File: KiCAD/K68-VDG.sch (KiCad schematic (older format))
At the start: 39 parts, among them J1 Video Out, J2 SBC6303 BUS, Q1 2SA1015, Q2 2SC1815, U1 MC6847, U2 MC1372, U3 74LS32, U4 74HCT573, U5 74LS02, U6 74LS244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

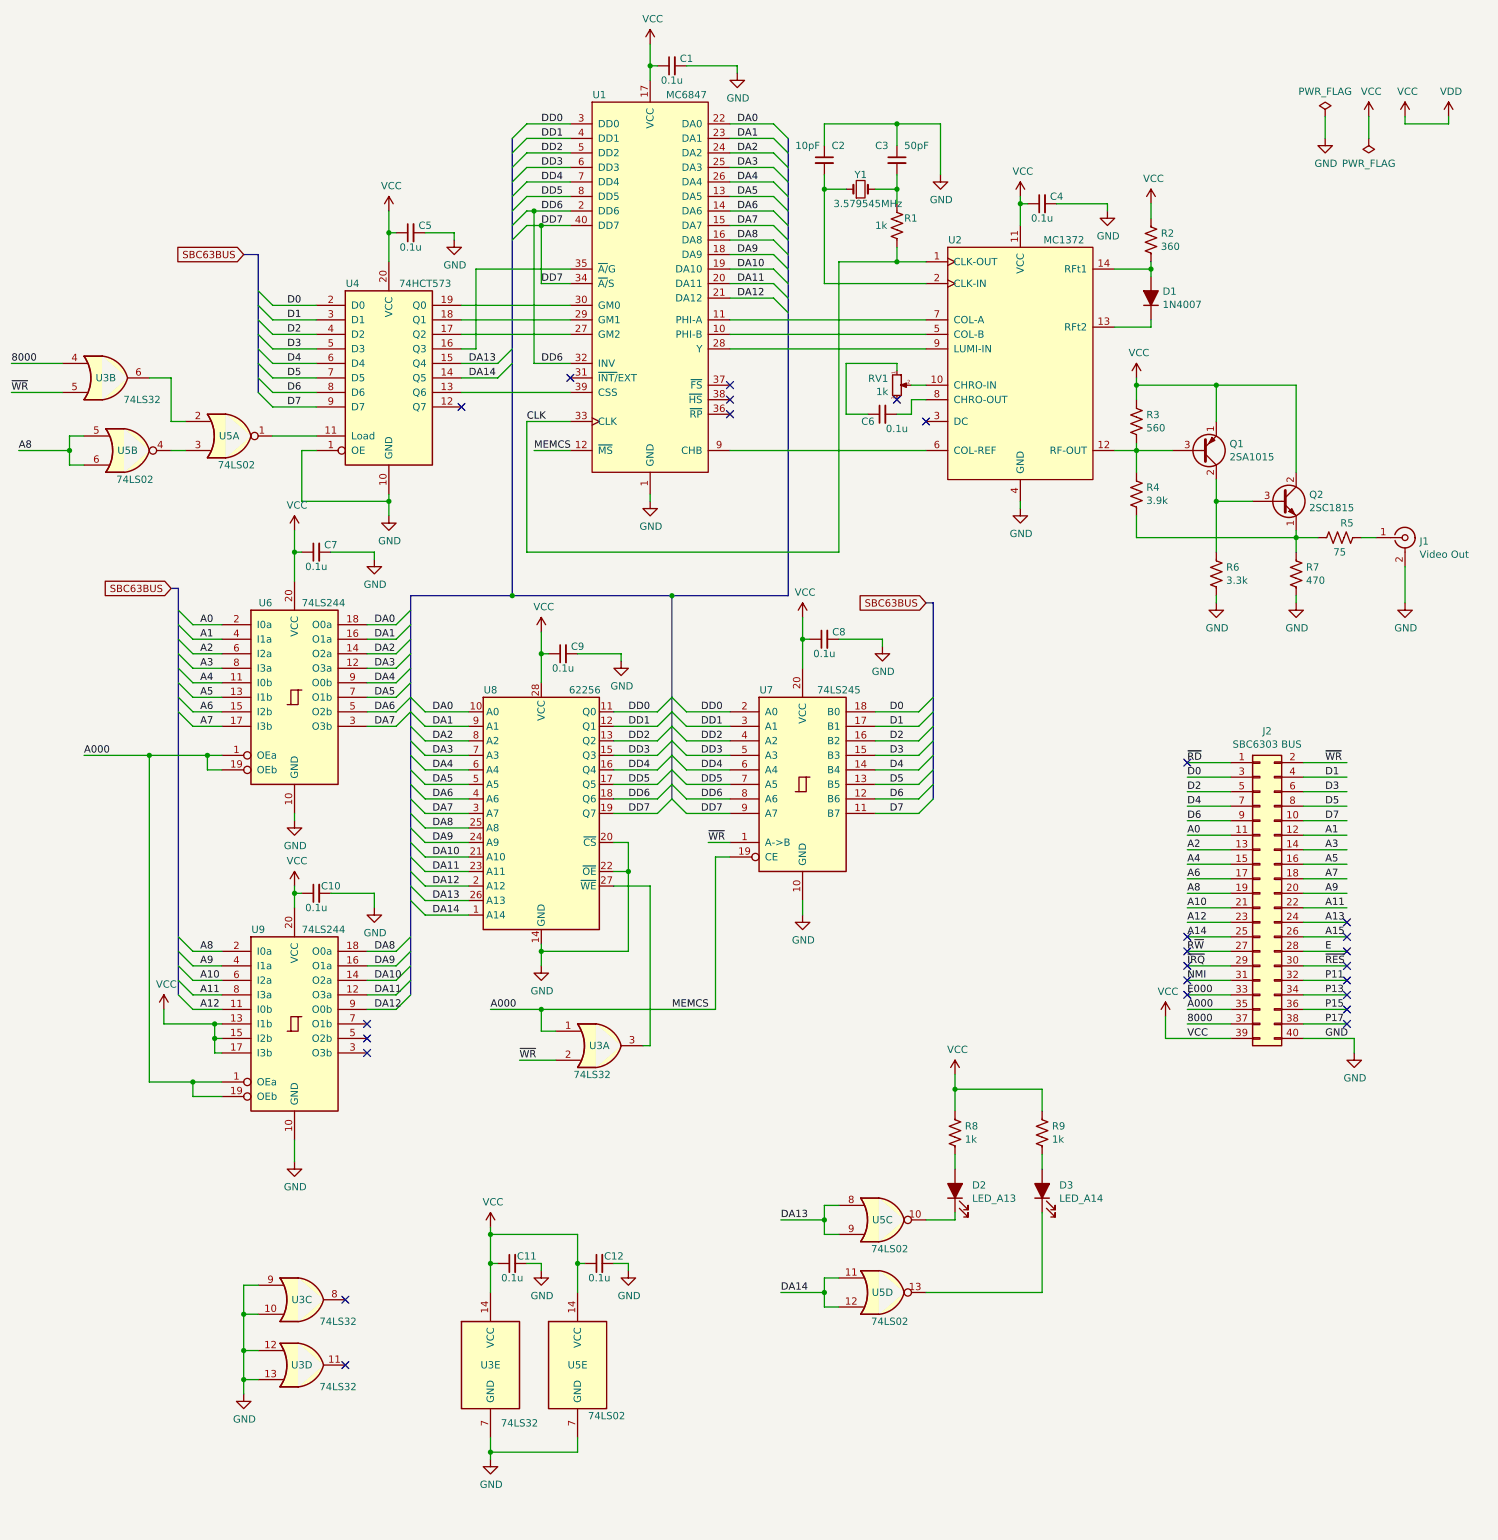
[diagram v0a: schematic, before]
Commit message: 回路修正、REV1基板ガーバーデータ出力
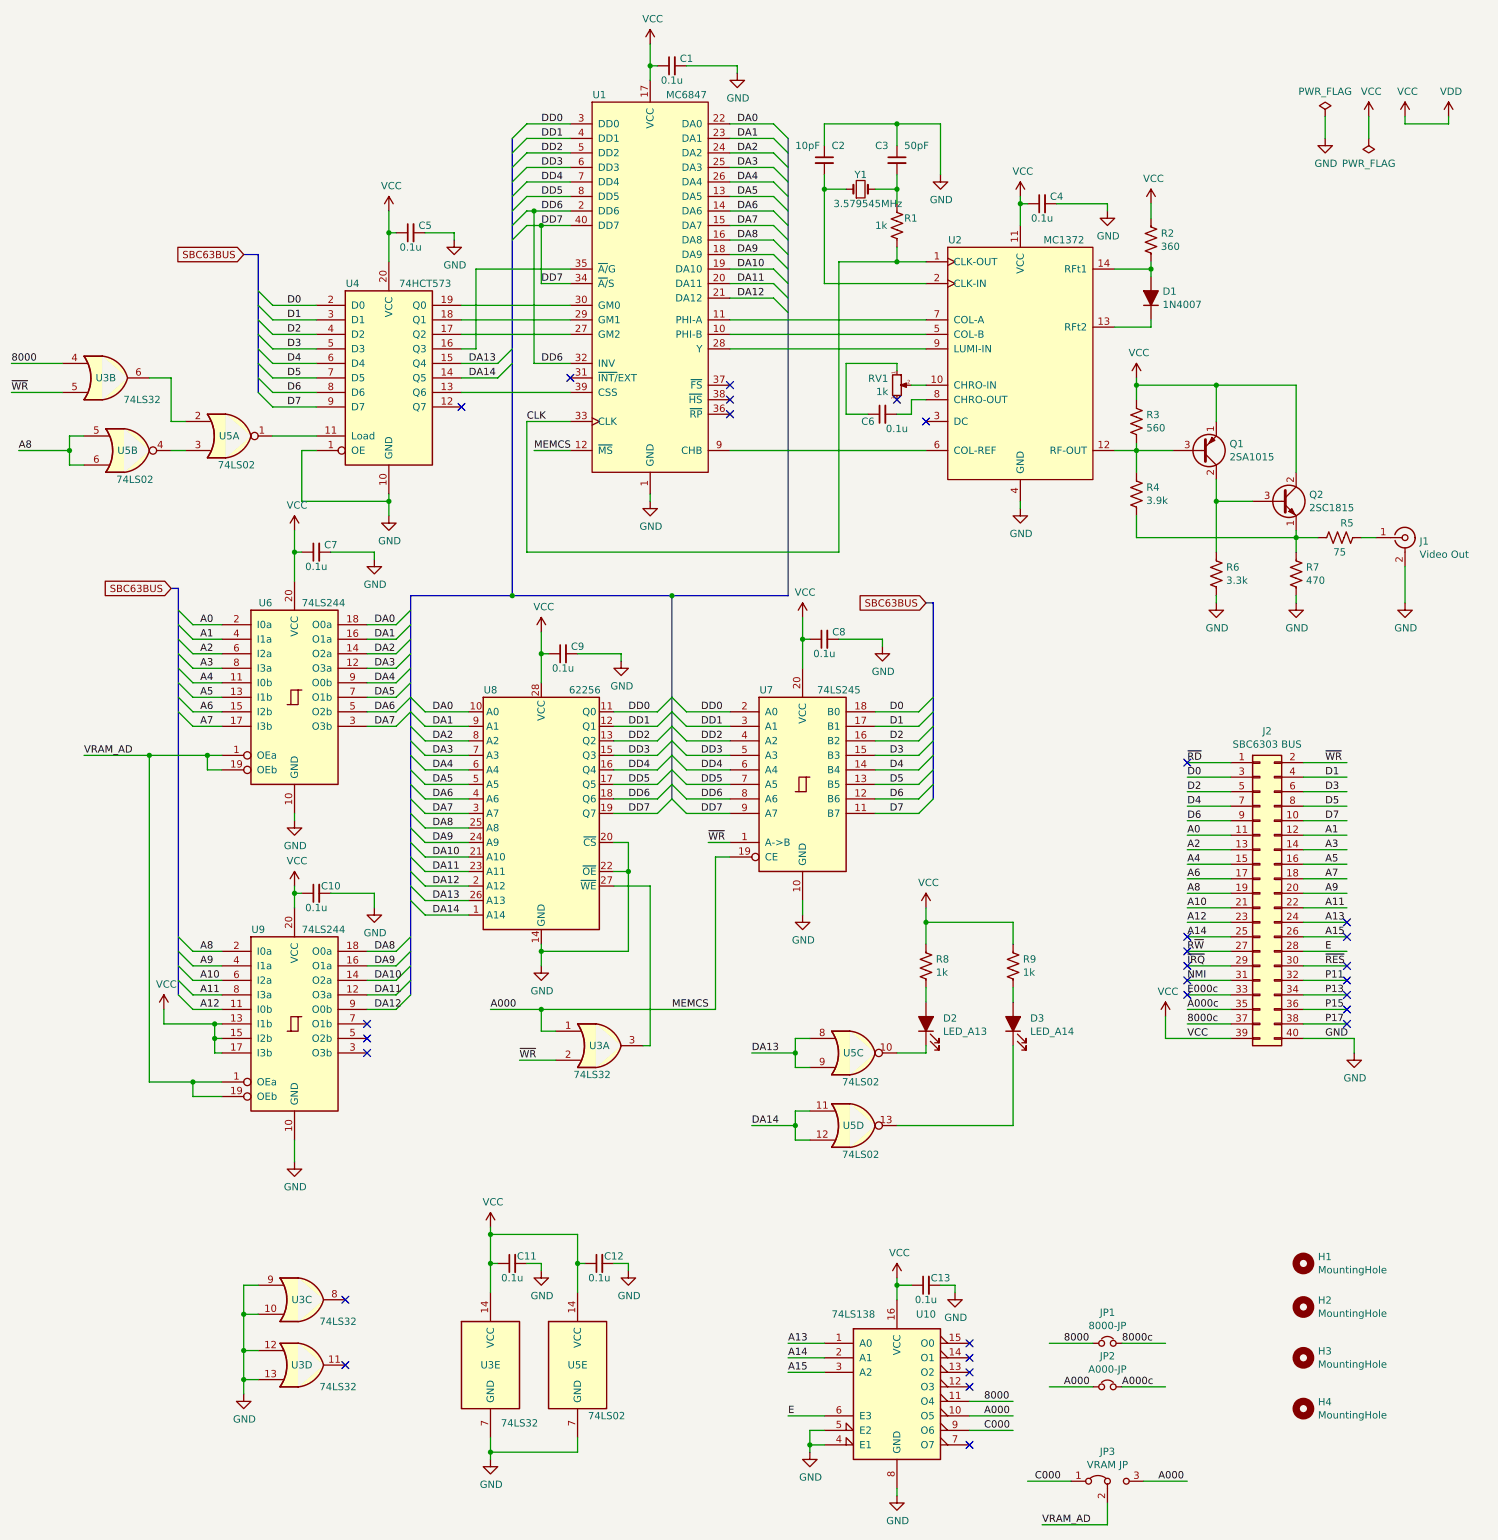
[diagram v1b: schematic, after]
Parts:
- added C13: 0.1u, Capacitor_THT:C_Disc_D3.0mm_W1.6mm_P2.50mm, symbol Device:C_Small
- added H1, H2, H3, H4: MountingHole, MountingHole:MountingHole_3.2mm_M3, symbol Mechanical:MountingHole
- added JP1: 8000-JP, Jumper:SolderJumper-2_P1.3mm_Open_RoundedPad1.0x1.5mm, symbol Device:Jumper_NC_Small
- added JP2: A000-JP, Jumper:SolderJumper-2_P1.3mm_Open_RoundedPad1.0x1.5mm, symbol Device:Jumper_NC_Small
- added JP3: VRAM JP, Jumper:SolderJumper-3_P1.3mm_Bridged12_RoundedPad1.0x1.5mm, symbol Jumper:Jumper_3_Bridged12
- added U10: 74LS138, Package_DIP:DIP-16_W7.62mm_Socket_LongPads, symbol 74xx:74LS138
- C1, C10, C11, C12, C2, C3, C4, C5, C6, C7, C8, C9: footprint (none) -> Capacitor_THT:C_Disc_D3.0mm_W1.6mm_P2.50mm
- D1: footprint (none) -> Diode_THT:D_DO-34_SOD68_P7.62mm_Horizontal
- D2, D3: footprint (none) -> LED_THT:LED_D3.0mm
- J1: footprint (none) -> RCA:RCAConAE
- J2: footprint (none) -> Connector_PinHeader_2.54mm:PinHeader_2x20_P2.54mm_Horizontal
- R1: footprint (none) -> Resistor_THT:R_Axial_DIN0207_L6.3mm_D2.5mm_P5.08mm_Vertical
- R2, R3, R4, R5, R6, R7, R8, R9: footprint (none) -> Resistor_THT:R_Axial_DIN0207_L6.3mm_D2.5mm_P10.16mm_Horizontal
- RV1: footprint (none) -> Potentiometer_THT:Potentiometer_Bourns_3386P_Vertical
- U1: footprint (none) -> Package_DIP:DIP-40_W15.24mm_Socket_LongPads
- U2, U3, U5: footprint (none) -> Package_DIP:DIP-14_W7.62mm_Socket_LongPads
- U4, U6, U7, U9: footprint (none) -> Package_DIP:DIP-20_W7.62mm_Socket_LongPads
- U8: footprint Package_DIP:DIP-28_W15.24mm -> Package_DIP:DIP-28_W15.24mm_Socket_LongPads
- Y1: footprint (none) -> Crystal:Crystal_HC49-U_Vertical
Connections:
- net labels added: 8000c, A000c, C000, E000c, VRAM_AD
- net labels removed: E000
- wire segments 352 -> 377
- no-connect marks 26 -> 30
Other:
- moved on the sheet: D2, D3, R8, R9, U5C, U5D
